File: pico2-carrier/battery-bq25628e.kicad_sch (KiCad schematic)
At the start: 21 parts, among them IC4 BQ25628ERYKR, Q1 DMG2305UX-7

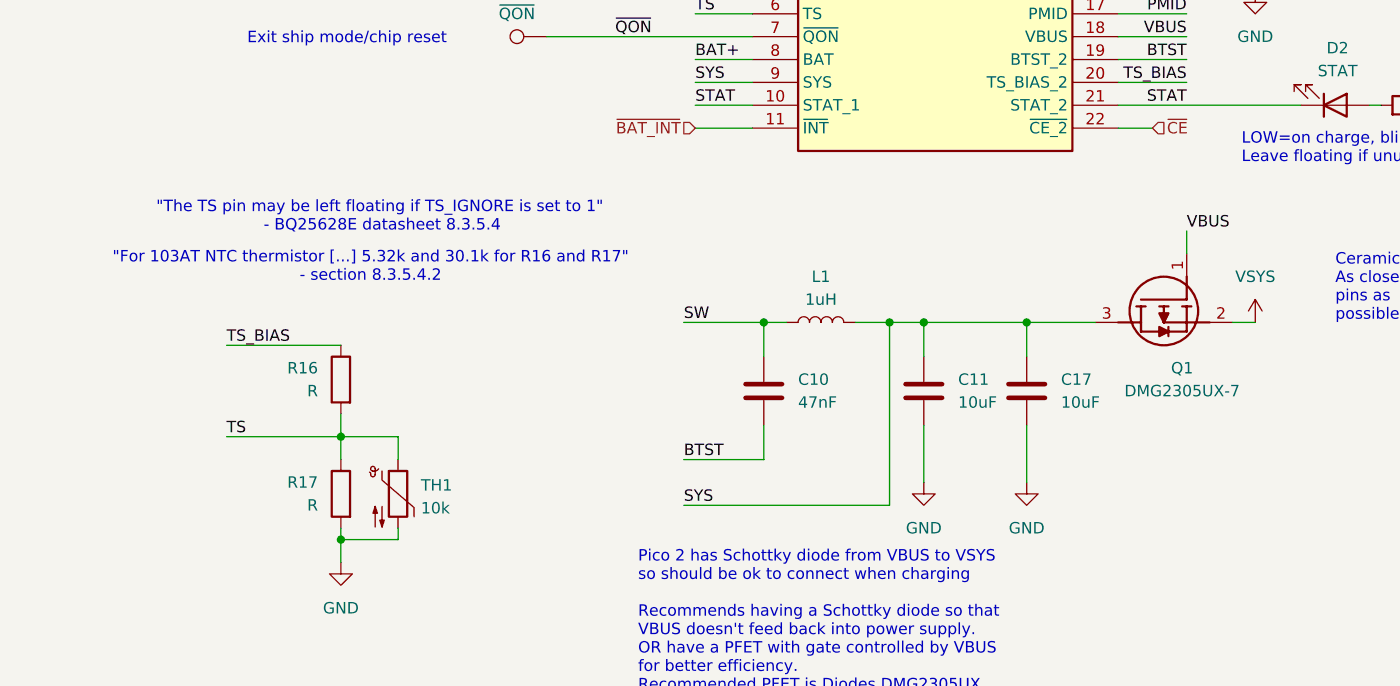
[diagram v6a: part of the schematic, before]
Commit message: carrier: update ir footprint
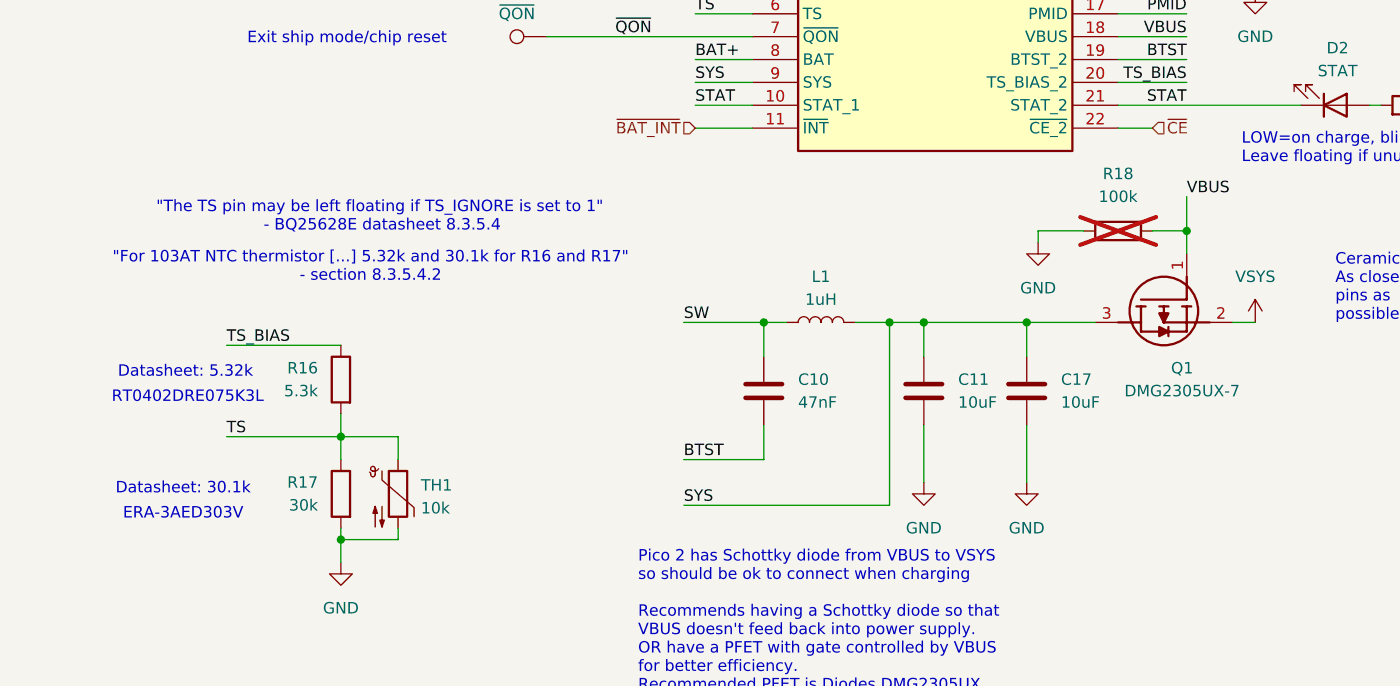
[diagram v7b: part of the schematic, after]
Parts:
- added R18: 100k, Resistor_SMD:R_0603_1608Metric, symbol Device:R
- R16: value R -> 5.3k
- R17: value R -> 30k; footprint Resistor_SMD:R_0402_1005Metric -> Resistor_SMD:R_0603_1608Metric
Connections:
- net GND: now also R18.1
- net VBUS: now also R18.2
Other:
- note added: "Datasheet: 30.1k"
- note added: "Datasheet: 5.32k"
- note added: "ERA-3AED303V"
- note added: "RT0402DRE075K3L"
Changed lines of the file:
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@@
 		(color 0 0 0 0)
 	)
+	(junction
+		(at 135.89 93.98)
+		(diameter 0)
+		(color 0 0 0 0)
+	)
 	(wire
 		(pts
@@
 	(wire
 		(pts
+			(xy 135.89 93.98) (xy 135.89 96.52)
+		)
+		(stroke
+			(width 0)
+			(type default)
+		)
+	)
+	(wire
+		(pts
+			(xy 124.46 93.98) (xy 119.38 93.98)
+		)
+		(stroke
+			(width 0)
+			(type default)
+		)
+	)
+	(wire
+		(pts
 			(xy 128.27 82.55) (xy 132.08 82.55)
 		)
@@
 	(wire
 		(pts
+			(xy 132.08 93.98) (xy 135.89 93.98)
+		)
+		(stroke
+			(width 0)
+			(type default)
+		)
+	)
+	(wire
+		(pts
 			(xy 81.28 64.77) (xy 87.63 64.77)
 		)
@@
 	(wire
 		(pts
-			(xy 135.89 93.98) (xy 135.89 96.52)
+			(xy 135.89 90.17) (xy 135.89 93.98)
 		)
 		(stroke
@@
 	(wire
 		(pts
+			(xy 119.38 93.98) (xy 119.38 95.25)
+		)
+		(stroke
+			(width 0)
+			(type default)
+		)
+	)
+	(wire
+		(pts
 			(xy 177.8 138.43) (xy 184.15 138.43)
 		)
@@
 		)
 	)
+	(text "RT0402DRE075K3L"
+		(exclude_from_sim no)
+		(at 24.892 112.522 0)
+		(effects
+			(font
+				(size 1.27 1.27)
+			)
+		)
+	)
 	(text "Rec. 10k resistor for pull-ups"
 		(exclude_from_sim no)
@@
 		)
 	)
+	(text "ERA-3AED303V"
+		(exclude_from_sim no)
+		(at 24.384 125.476 0)
+		(effects
+			(font
+				(size 1.27 1.27)
+			)
+		)
+	)
+	(text "Datasheet: 5.32k"
+		(exclude_from_sim no)
+		(at 24.638 109.728 0)
+		(effects
+			(font
+				(size 1.27 1.27)
+			)
+		)
+	)
 	(text "For pkcell 500mAh LP503035:\nStandard charge 0.2C, quick charge 1C\nCut off current 0.01C\nMax discharge 1C\nJST-PH-2P Counterparts:\n- B2B-PH-K-S (Top-entry THT, cheap ~£0.15)\n- S2B-PH-SM4-TB (Side-entry SMD, more expensive ~£0.45)"
 		(exclude_from_sim no)
@@
 		)
 	)
+	(text "Datasheet: 30.1k"
+		(exclude_from_sim no)
+		(at 24.384 122.682 0)
+		(effects
+			(font
+				(size 1.27 1.27)
+			)
+		)
+	)
 	(text "Can be software disabled"
 		(exclude_from_sim no)
@@
 	)
 	(label "VBUS"
-		(at 135.89 93.98 0)
+		(at 135.89 90.17 0)
 		(fields_autoplaced yes)
 		(effects
@@
 	)
 	(symbol
+		(lib_id "Device:R")
+		(at 128.27 93.98 90)
+		(unit 1)
+		(exclude_from_sim no)
+		(in_bom yes)
+		(on_board yes)
+		(dnp yes)
+		(fields_autoplaced yes)
+		(property "Reference" "R18"
+			(at 128.27 87.63 90)
+			(effects
+				(font
+					(size 1.27 1.27)
+				)
+			)
+		)
+		(property "Value" "100k"
+			(at 128.27 90.17 90)
+			(effects
+				(font
+					(size 1.27 1.27)
+				)
+			)
+		)
+		(property "Footprint" "Resistor_SMD:R_0603_1608Metric"
+			(at 128.27 95.758 90)
+			(effects
+				(font
+					(size 1.27 1.27)
+				)
+				(hide yes)
+			)
+		)
+		(property "Datasheet" "~"
+			(at 128.27 93.98 0)
+			(effects
+				(font
+					(size 1.27 1.27)
+				)
+				(hide yes)
+			)
+		)
+		(property "Description" "Resistor"
+			(at 128.27 93.98 0)
+			(effects
+				(font
+					(size 1.27 1.27)
+				)
+				(hide yes)
+			)
+		)
+		(pin "1"
+		)
+		(pin "2"
+		)
+		(instances
+			(project ""
+				(path "/4204b4ad-0ae5-4a8a-a079-fb4cf2b0ed9e/186b40c8-acb6-4b31-a880-ca87c0770f9c"
+					(reference "R18")
+					(unit 1)
+				)
+			)
+		)
+	)
+	(symbol
 		(lib_id "Device:L")
 		(at 95.25 104.14 90)
@@
 	)
 	(symbol
+		(lib_id "power:GND")
+		(at 119.38 95.25 0)
+		(unit 1)
+		(exclude_from_sim no)
+		(in_bom yes)
+		(on_board yes)
+		(dnp no)
+		(fields_autoplaced yes)
+		(property "Reference" "#PWR069"
+			(at 119.38 101.6 0)
+			(effects
+				(font
+					(size 1.27 1.27)
+				)
+				(hide yes)
+			)
+		)
+		(property "Value" "GND"
+			(at 119.38 100.33 0)
+			(effects
+				(font
+					(size 1.27 1.27)
+				)
+			)
+		)
+		(property "Footprint" ""
+			(at 119.38 95.25 0)
+			(effects
+				(font
+					(size 1.27 1.27)
+				)
+				(hide yes)
+			)
+		)
+		(property "Datasheet" ""
+			(at 119.38 95.25 0)
+			(effects
+				(font
+					(size 1.27 1.27)
+				)
+				(hide yes)
+			)
+		)
+		(property "Description" ""
+			(at 119.38 95.25 0)
+			(effects
+				(font
+					(size 1.27 1.27)
+				)
+				(hide yes)
+			)
+		)
+		(pin "1"
+		)
+		(instances
+			(project "pico2-carrier"
+				(path "/4204b4ad-0ae5-4a8a-a079-fb4cf2b0ed9e/186b40c8-acb6-4b31-a880-ca87c0770f9c"
+					(reference "#PWR069")
+					(unit 1)
+				)
+			)
+		)
+	)
+	(symbol
 		(lib_id "Device:R")
 		(at 41.91 110.49 0)
@@
 			)
 		)
-		(property "Value" "R"
+		(property "Value" "5.3k"
 			(at 39.37 111.7599 0)
 			(effects
@@
 			)
 		)
-		(property "Value" "R"
+		(property "Value" "30k"
 			(at 39.37 124.4599 0)
 			(effects
@@
 			)
 		)
-		(property "Footprint" "Resistor_SMD:R_0402_1005Metric"
+		(property "Footprint" "Resistor_SMD:R_0603_1608Metric"
 			(at 43.688 123.19 90)
 			(effects

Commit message: v0.1: files housekeeping
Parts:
- TH1: footprint Resistor_SMD:R_0603_1608Metric -> Resistor_SMD:R_0402_1005Metric
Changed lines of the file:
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@@
 			)
 		)
-		(property "Footprint" "Resistor_SMD:R_0603_1608Metric"
+		(property "Footprint" "Resistor_SMD:R_0402_1005Metric"
 			(at 48.26 121.92 0)
 			(effects
